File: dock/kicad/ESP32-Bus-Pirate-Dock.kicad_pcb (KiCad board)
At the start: 4 copper layers, 80 x 73.8 mm, 49 parts, among them CN1 HX25418-10WA, J1 Conn_01x22, J2 Conn_01x22, J3 Conn_01x10V, J4 Conn_01x22, J5 Conn_01x22, J6 Conn_01x22, J7 Conn_02x03, J8 TC2050, Q1 2SK2009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

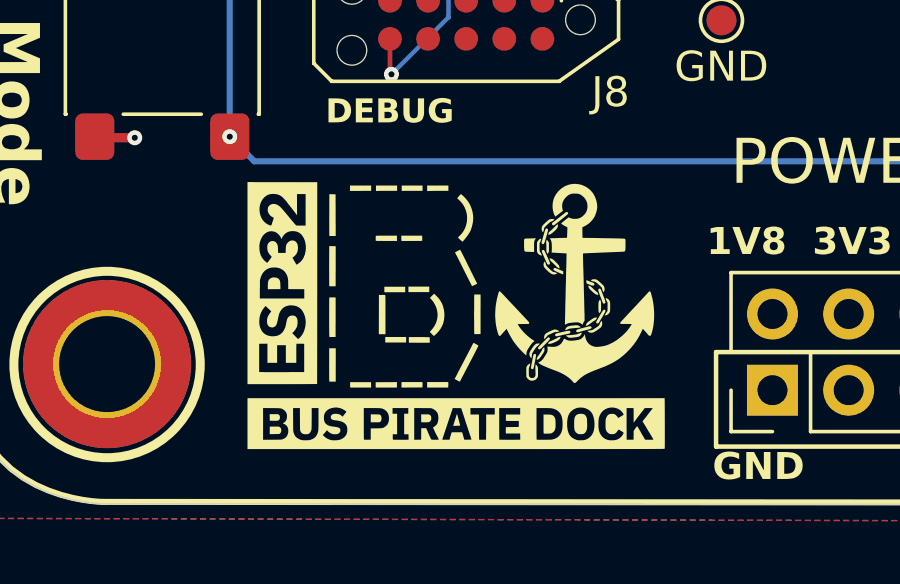
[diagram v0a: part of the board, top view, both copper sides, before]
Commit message: Changed logo
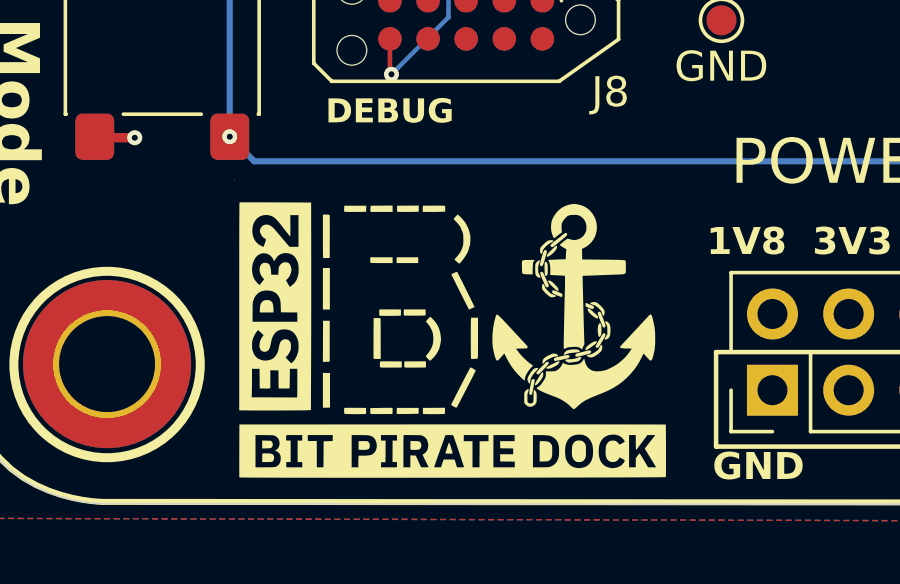
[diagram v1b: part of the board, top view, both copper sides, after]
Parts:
- moved G*** 0.43 mm to (76.5, 136.5)
